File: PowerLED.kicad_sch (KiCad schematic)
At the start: 3 parts

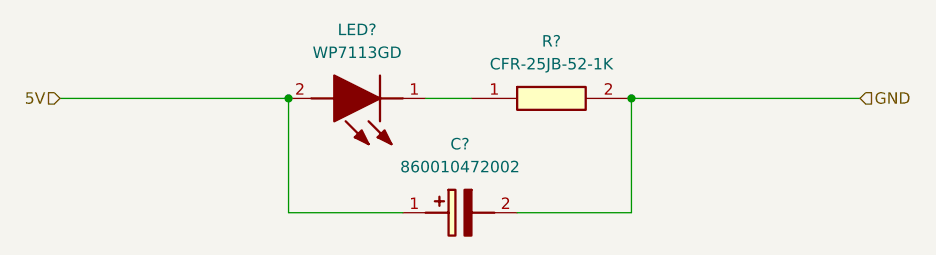
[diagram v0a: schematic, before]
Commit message: Updated re-annotated the schematics, created new PCB based on standards and updated components.
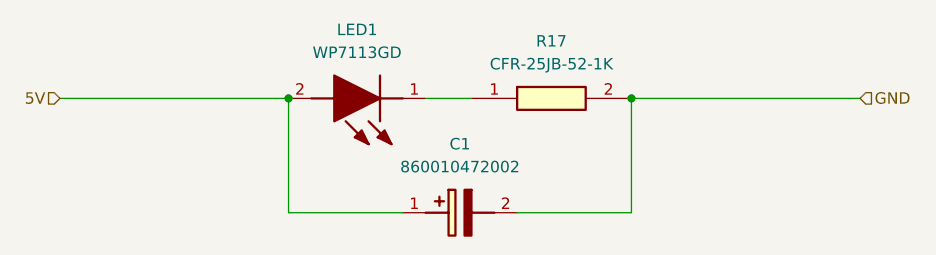
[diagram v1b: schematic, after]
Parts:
- R17: renamed from R?; footprint SamacSys_Parts:RESAD1590W60L630D240 -> Resistor_THT:R_Axial_DIN0204_L3.6mm_D1.6mm_P7.62mm_Horizontal
- gave numbers to parts that had none: 2
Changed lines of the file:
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@@
 		(dnp no)
 		(fields_autoplaced yes)
-		(property "Reference" "LED?"
+		(property "Reference" "LED1"
 			(at 134.62 93.98 0)
 			(effects
@@
 			(project "Arduino Light Controller"
 				(path "/1ab818d2-1673-4bd5-b77a-2cfddf9e3efa/2640229e-9cdb-4ca5-b402-47f6738a7a82"
-					(reference "LED?")
+					(reference "LED1")
 					(unit 1)
 				)
@@
 		(dnp no)
 		(fields_autoplaced yes)
-		(property "Reference" "R?"
+		(property "Reference" "R17"
 			(at 156.21 95.25 0)
 			(effects
@@
 			)
 		)
-		(property "Footprint" "SamacSys_Parts:RESAD1590W60L630D240"
+		(property "Footprint" "Resistor_THT:R_Axial_DIN0204_L3.6mm_D1.6mm_P7.62mm_Horizontal"
 			(at 161.29 197.79 0)
 			(effects
@@
 			(project "Arduino Light Controller"
 				(path "/1ab818d2-1673-4bd5-b77a-2cfddf9e3efa/2640229e-9cdb-4ca5-b402-47f6738a7a82"
-					(reference "R?")
+					(reference "R17")
 					(unit 1)
 				)
@@
 		(dnp no)
 		(fields_autoplaced yes)
-		(property "Reference" "C?"
+		(property "Reference" "C1"
 			(at 146.05 106.68 0)
 			(effects
@@
 			(project "Arduino Light Controller"
 				(path "/1ab818d2-1673-4bd5-b77a-2cfddf9e3efa/2640229e-9cdb-4ca5-b402-47f6738a7a82"
-					(reference "C?")
+					(reference "C1")
 					(unit 1)
 				)

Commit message: Updated components to the custom library and applied additional standards.
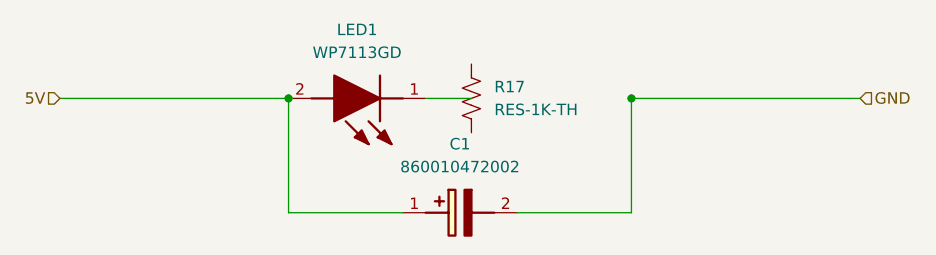
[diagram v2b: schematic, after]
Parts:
- R17: value CFR-25JB-52-1K -> RES-1K-TH; symbol SamacSys_Parts:CFR-25JB-52-1K -> Custom:Res-1K-TH; Manufacturer_Name KEMET -> YAGEO; Manufacturer_Part_Number CFR-25JB-52-1K -> CFR-25JR-52-1K; Supplier (none) -> Mouser; Supplier Part Number (none) -> 603-CFR-25JR-521K; Supplier Price/Stock (none) -> https://www.mouser.com/ProductDetail/YAGEO/CFR-25JR-52-1K?q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
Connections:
- net GND: no longer R17.2
- net at LED1.1 (K): no longer R17.1
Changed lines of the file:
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@@
 	)
 	(symbol
-		(lib_id "SamacSys_Parts:CFR-25JB-52-1K")
+		(lib_id "Custom:Res-1K-TH")
 		(at 147.32 101.6 0)
 		(unit 1)
@@
 		(fields_autoplaced yes)
 		(property "Reference" "R17"
-			(at 156.21 95.25 0)
+			(at 149.86 100.3299 0)
 			(effects
 				(font
 					(size 1.27 1.27)
 				)
+				(justify left)
 			)
 		)
-		(property "Value" "CFR-25JB-52-1K"
-			(at 156.21 97.79 0)
+		(property "Value" "RES-1K-TH"
+			(at 149.86 102.8699 0)
 			(effects
 				(font
 					(size 1.27 1.27)
 				)
+				(justify left)
 			)
 		)
 		(property "Footprint" "Resistor_THT:R_Axial_DIN0204_L3.6mm_D1.6mm_P7.62mm_Horizontal"
-			(at 161.29 197.79 0)
+			(at 148.336 101.854 90)
 			(effects
 				(font
 					(size 1.27 1.27)
 				)
-				(justify left top)
 				(hide yes)
 			)
 		)
-		(property "Datasheet" ""
-			(at 161.29 297.79 0)
+		(property "Datasheet" "https://www.mouser.com/datasheet/3/508/1/YAGEO%20CFR_datasheet_2023v2.pdf"
+			(at 147.32 101.6 0)
 			(effects
 				(font
 					(size 1.27 1.27)
 				)
-				(justify left top)
 				(hide yes)
 			)
 		)
-		(property "Description" "Carbon Film Resistors - Through Hole 1/4W 1K Ohm 5%"
+		(property "Description" "Resistor - 1K- 1/4W - 5% - Through Hole"
 			(at 147.32 101.6 0)
 			(effects
@@
 			)
 		)
-		(property "Manufacturer_Name" "KEMET"
-			(at 161.29 797.79 0)
+		(property "Manufacturer_Name" "YAGEO"
+			(at 147.32 101.6 0)
 			(effects
 				(font
 					(size 1.27 1.27)
 				)
-				(justify left top)
 				(hide yes)
 			)
 		)
-		(property "Manufacturer_Part_Number" "CFR-25JB-52-1K"
-			(at 161.29 897.79 0)
+		(property "Manufacturer_Part_Number" "CFR-25JR-52-1K "
+			(at 147.32 101.6 0)
 			(effects
 				(font
 					(size 1.27 1.27)
 				)
-				(justify left top)
 				(hide yes)
 			)
+		)
+		(property "Supplier" "Mouser"
+			(at 147.32 101.6 0)
+			(effects
+				(font
+					(size 1.27 1.27)
+				)
+				(hide yes)
+			)
+		)
+		(property "Supplier Part Number" "603-CFR-25JR-521K"
+			(at 147.32 101.6 0)
+			(effects
+				(font
+					(size 1.27 1.27)
+				)
+				(hide yes)
+			)
+		)
+		(property "Supplier Price/Stock" "https://www.mouser.com/ProductDetail/YAGEO/CFR-25JR-52-1K?qs=FK4oyhsNhknmd5zXOZ4mTQ%3D%3D"
+			(at 147.32 101.6 0)
+			(effects
+				(font
+					(size 1.27 1.27)
+				)
+				(hide yes)
+			)

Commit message: Updated sheets with title, version, and date.  Corrected issue with resistor placement and connection on PowerLED module.
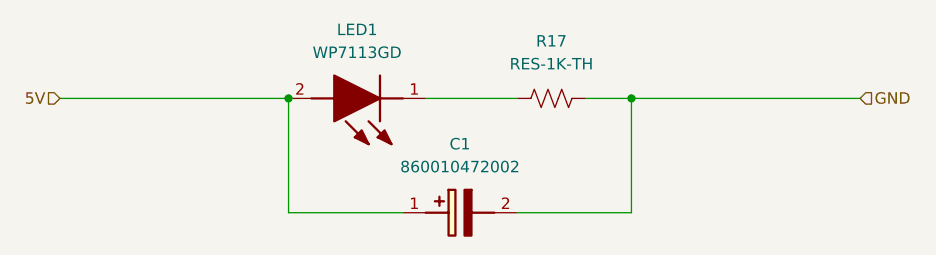
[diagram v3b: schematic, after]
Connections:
- net GND: now also R17.2
- net at LED1.1 (K): now also R17.1
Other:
- title: (none) -> Arduino Light Controller - Power LED Module
- moved on the sheet: R17
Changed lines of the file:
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@@
 	(generator_version "9.0")
 	(paper "A4")
+	(title_block
+		(title "Arduino Light Controller - Power LED Module")
+		(date "2026-01-30")
+		(rev "1.1")
+	)
 	(junction
 		(at 127 101.6)
@@
 	(wire
 		(pts
-			(xy 142.24 101.6) (xy 147.32 101.6)
+			(xy 142.24 101.6) (xy 152.4 101.6)
 		)
 		(stroke
@@
 		(pts
 			(xy 101.6 101.6) (xy 127 101.6)
+		)
+		(stroke
+			(width 0)
+			(type default)
+		)
+	)
+	(wire
+		(pts
+			(xy 160.02 101.6) (xy 165.1 101.6)
 		)
 		(stroke
@@
 	(symbol
 		(lib_id "Custom:Res-1K-TH")
-		(at 147.32 101.6 0)
+		(at 156.21 101.6 90)
 		(unit 1)
 		(exclude_from_sim no)
@@
 		(fields_autoplaced yes)
 		(property "Reference" "R17"
-			(at 149.86 100.3299 0)
-			(effects
-				(font
-					(size 1.27 1.27)
-				)
-				(justify left)
+			(at 156.21 95.25 90)
+			(effects
+				(font
+					(size 1.27 1.27)
+				)
 			)
 		)
 		(property "Value" "RES-1K-TH"
-			(at 149.86 102.8699 0)
-			(effects
-				(font
-					(size 1.27 1.27)
-				)
-				(justify left)
+			(at 156.21 97.79 90)
+			(effects
+				(font
+					(size 1.27 1.27)
+				)
 			)
 		)
 		(property "Footprint" "Resistor_THT:R_Axial_DIN0204_L3.6mm_D1.6mm_P7.62mm_Horizontal"
-			(at 148.336 101.854 90)
+			(at 156.464 100.584 90)
 			(effects
 				(font
@@
 		)
 		(property "Datasheet" "https://www.mouser.com/datasheet/3/508/1/YAGEO%20CFR_datasheet_2023v2.pdf"
-			(at 147.32 101.6 0)
+			(at 156.21 101.6 0)
 			(effects
 				(font
@@
 		)
 		(property "Description" "Resistor - 1K- 1/4W - 5% - Through Hole"
-			(at 147.32 101.6 0)
+			(at 156.21 101.6 0)
 			(effects
 				(font
@@
 		)
 		(property "Height" ""
-			(at 161.29 497.79 0)
+			(at 552.4 87.63 0)
 			(effects
 				(font
@@
 		)
 		(property "Mouser Part Number" "N/A"
-			(at 161.29 597.79 0)
+			(at 652.4 87.63 0)
 			(effects
 				(font
@@
 		)
 		(property "Mouser Price/Stock" "https://www.mouser.co.uk/ProductDetail/Yageo/CFR-25JB-52-1K/?qs=oypCK0zG326Dzm6bUFS4DQ%3D%3D"
-			(at 161.29 697.79 0)
+			(at 752.4 87.63 0)
 			(effects
 				(font
@@
 		)
 		(property "Manufacturer_Name" "YAGEO"
-			(at 147.32 101.6 0)
+			(at 156.21 101.6 0)
 			(effects
 				(font
@@
 		)
 		(property "Manufacturer_Part_Number" "CFR-25JR-52-1K "
-			(at 147.32 101.6 0)
+			(at 156.21 101.6 0)
 			(effects
 				(font
@@
 		)
 		(property "Supplier" "Mouser"
-			(at 147.32 101.6 0)
+			(at 156.21 101.6 0)
 			(effects
 				(font
@@
 		)
 		(property "Supplier Part Number" "603-CFR-25JR-521K"
-			(at 147.32 101.6 0)
+			(at 156.21 101.6 0)
 			(effects
 				(font
@@
 		)
 		(property "Supplier Price/Stock" "https://www.mouser.com/ProductDetail/YAGEO/CFR-25JR-52-1K?qs=FK4oyhsNhknmd5zXOZ4mTQ%3D%3D"
-			(at 147.32 101.6 0)
-			(effects
-				(font
+			(at 156.21 101.6 0)
+			(effects
+				(font

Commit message: Missed updating PowerLED module with components from the custom library.
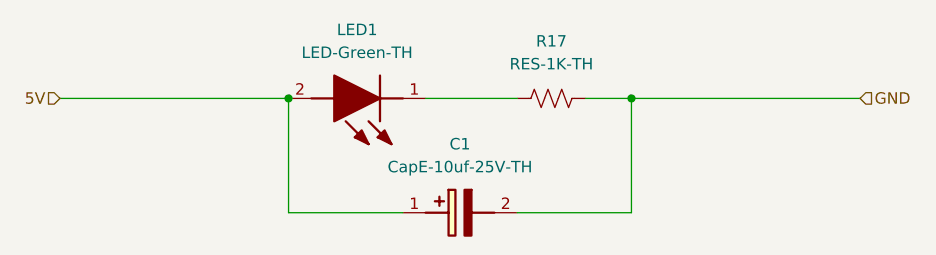
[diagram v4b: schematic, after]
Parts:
- C1: value 860010472002 -> CapE-10uf-25V-TH; footprint SamacSys_Parts:CAPPRD200W52D500H1250 -> Custom:710-860010472002; symbol SamacSys_Parts:860010472002 -> Custom:CapE-10uf-25V-TH; Supplier (none) -> Mouser; Supplier Part Number (none) -> 710-860010472002; Supplier Price/Stock (none) -> https://www.mouser.co.uk/ProductDetail/Wurth-Elektronik/860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
- LED1: value WP7113GD -> LED-Green-TH; footprint SamacSys_Parts:L53ND -> Custom:604-WP7113GD; symbol SamacSys_Parts:WP7113GD -> Custom:LED-Green-TH; Supplier (none) -> Mouser; Supplier Part Number (none) -> 604-WP7113GD; Supplier Price/Stock (none) -> https://www.mouser.co.uk/ProductDetail/Kingbright/WP7113GD?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
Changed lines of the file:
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@@
 	)
 	(symbol
-		(lib_id "SamacSys_Parts:WP7113GD")
+		(lib_id "Custom:LED-Green-TH")
 		(at 142.24 101.6 180)
 		(unit 1)
@@
 			)
 		)
-		(property "Value" "WP7113GD"
+		(property "Value" "LED-Green-TH"
 			(at 134.62 96.52 0)
 			(effects
@@
 			)
 		)
-		(property "Footprint" "SamacSys_Parts:L53ND"
+		(property "Footprint" "Custom:604-WP7113GD"
 			(at 129.54 7.95 0)
 			(effects
@@
 			)
 		)
-		(property "Description" "Standard LEDs - Through Hole GREEN DIFFUSED"
+		(property "Description" "LED - Through Hole GREEN DIFFUSED"
 			(at 142.24 101.6 0)
 			(effects
@@
 		(property "Manufacturer_Part_Number" "WP7113GD"
 			(at 129.54 -692.05 0)
+			(effects
+				(font
+					(size 1.27 1.27)
+				)
+				(justify left bottom)
+				(hide yes)
+			)
+		)
+		(property "Supplier" "Mouser"
+			(at 142.24 101.6 0)
+			(effects
+				(font
+					(size 1.27 1.27)
+				)
+				(hide yes)
+			)
+		)
+		(property "Supplier Part Number" "604-WP7113GD"
+			(at 129.54 -392.05 0)
+			(effects
+				(font
+					(size 1.27 1.27)
+				)
+				(justify left bottom)
+				(hide yes)
+			)
+		)
+		(property "Supplier Price/Stock" "https://www.mouser.co.uk/ProductDetail/Kingbright/WP7113GD?qs=pz0eHrWKk7njL1kTYKysuw%3D%3D"
+			(at 129.54 -492.05 0)
 			(effects
 				(font
@@
 	)
 	(symbol
-		(lib_id "SamacSys_Parts:860010472002")
+		(lib_id "Custom:CapE-10uf-25V-TH")
 		(at 139.7 114.3 0)
 		(unit 1)
@@
 			)
 		)
-		(property "Value" "860010472002"
+		(property "Value" "CapE-10uf-25V-TH"
 			(at 146.05 109.22 0)
 			(effects
@@
 			)
 		)
-		(property "Footprint" "SamacSys_Parts:CAPPRD200W52D500H1250"
+		(property "Footprint" "Custom:710-860010472002"
 			(at 148.59 210.49 0)
 			(effects
@@
 			(effects
 				(font
+					(size 1.27 1.27)
+				)
+				(justify left top)
+				(hide yes)
+			)
+		)
+		(property "Supplier" "Mouser"
+			(at 139.7 114.3 0)
+			(effects
+				(font
+					(size 1.27 1.27)
+				)
+				(hide yes)
+			)
+		)
+		(property "Supplier Part Number" "710-860010472002"
+			(at 148.59 610.49 0)
+			(effects
+				(font
+					(size 1.27 1.27)
+				)
+				(justify left top)
+				(hide yes)
+			)
+		)
+		(property "Supplier Price/Stock" "https://www.mouser.co.uk/ProductDetail/Wurth-Elektronik/860010472002?qs=0KOYDY2FL2%2FyXlauDHcLjg%3D%3D"
+			(at 148.59 710.49 0)
+			(effects
+				(font
